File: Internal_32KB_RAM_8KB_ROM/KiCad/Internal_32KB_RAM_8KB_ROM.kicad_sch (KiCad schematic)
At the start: 12 parts, among them J1 UD4, J2 UE4, J3 RAM Decoder, J4 BLK Decoder, J5 Disable/Enable Switch, U1 ATF16V8, U2 74HCT138, U3 62256

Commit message: Redesigning
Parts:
- added C4: 100nF, Capacitor_THT:C_Disc_D3.0mm_W2.0mm_P2.50mm, symbol Device:C
- added U4: 2864, Package_DIP:DIP-28_W15.24mm, symbol Memory_EEPROM:KM28C64A
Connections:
- net +5V: now also C4.1, U4.27 (~{WE}), U4.28 (VCC)
- net BD0: now also U4.11 (I/O0)
- net BD1: now also U4.12 (I/O1)
- net BD2: now also U4.13 (I/O2)
- net BD3: now also U4.15 (I/O3)
- net BD4: now also U4.16 (I/O4)
- net BD5: now also U4.17 (I/O5)
- net BD6: now also U4.18 (I/O6)
- net BD7: now also U4.19 (I/O7)
- net GND: now also C4.2, U4.14 (GND), U4.22 (~{OE})
- net RAM_A13: now also U1.14 (I/O); no longer U1.13 (I/O)
- net RAM_A14: now also U1.15 (I/O); no longer U1.14 (I/O)
- net VA0: now also U4.10 (A0)
- net VA1: now also U4.9 (A1)
- net VA10: now also U4.21 (A10)
- net VA11: now also U4.23 (A11)
- net VA12: now also U4.2 (A12)
- net VA2: now also U4.8 (A2)
- net VA3: now also U4.7 (A3)
- net VA4: now also U4.6 (A4)
- net VA5: now also U4.5 (A5)
- net VA6: now also U4.4 (A6)
- net VA7: now also U4.3 (A7)
- net VA8: now also U4.25 (A8)
- net VA9: now also U4.24 (A9)
- net VR/~{W}: now also J1.10 (Pin_10); no longer J2.10 (Pin_10)
- net ~{BLK5_OUT}: now also U1.12 (I/O), U4.20 (~{CE}); no longer U1.15 (I/O)
- net ~{RAM_CS}: now also U1.13 (I/O); no longer U1.12 (I/O)
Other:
- note removed: "Future: To support ~{BLK5} expansion we will need to add an additional 6264"
- title: Commodore VIC-20 32KB RAM Expansion  -> Commodore VIC-20 32KB RAM+ROM Expansion 

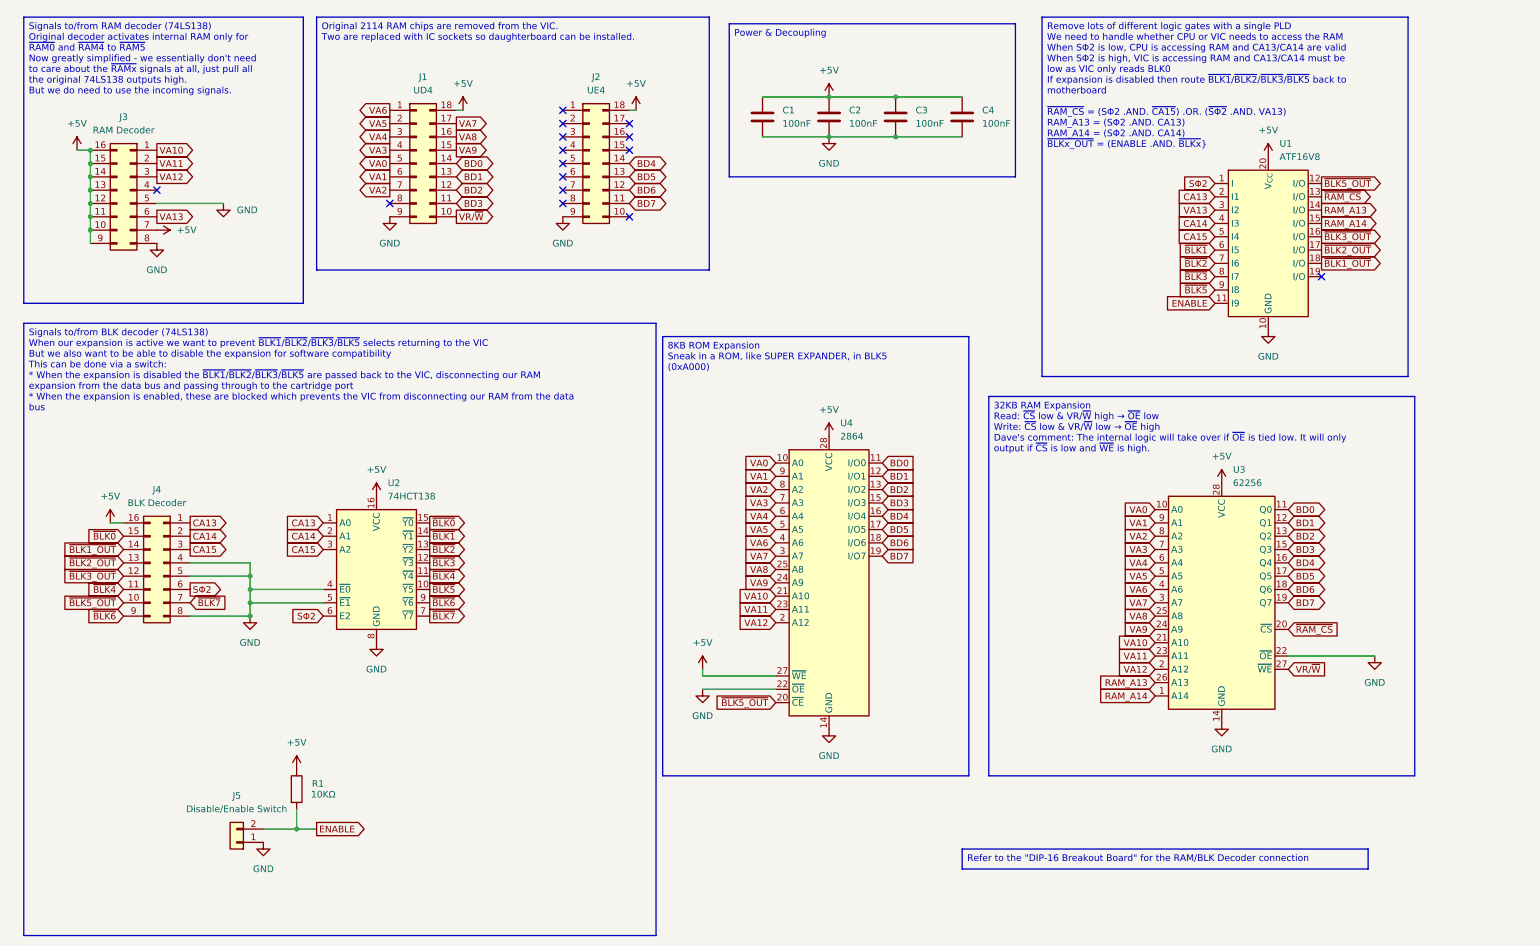
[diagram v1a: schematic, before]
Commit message: Finalised 40KB design for testing
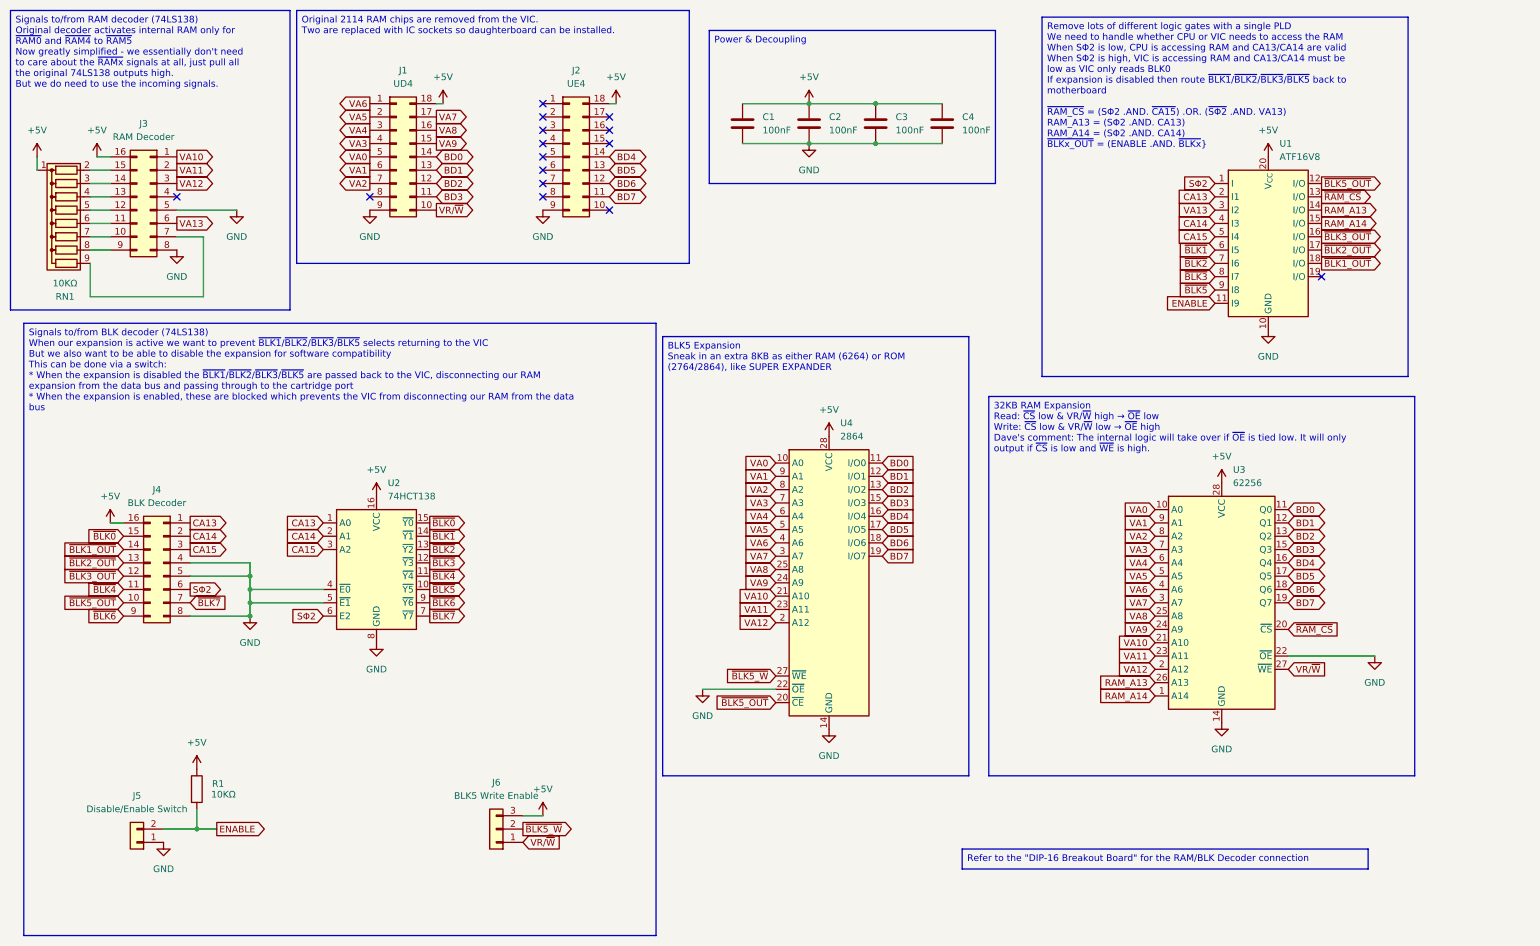
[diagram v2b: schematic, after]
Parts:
- added J6: BLK5 Write Enable, Connector_PinHeader_2.54mm:PinHeader_1x03_P2.54mm_Vertical, symbol Connector_Generic:Conn_01x03
- added RN1: 10KΩ, Resistor_THT:R_Array_SIP9, symbol Device:R_Network08
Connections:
- net +5V: now also J6.3 (Pin_3), RN1.1 (common); no longer J3.10 (Pin_10), J3.11 (Pin_11), J3.12 (Pin_12), J3.13 (Pin_13), J3.14 (Pin_14), J3.15 (Pin_15), J3.7 (Pin_7), J3.9 (Pin_9), U4.27 (~{WE})
- net VR/~{W}: now also J6.1 (Pin_1)
- new net: J3.10 (Pin_10), RN1.7 (R6)
- new net: J3.11 (Pin_11), RN1.6 (R5)
- new net: J3.12 (Pin_12), RN1.5 (R4)
- new net: J3.13 (Pin_13), RN1.4 (R3)
- new net: J3.14 (Pin_14), RN1.3 (R2)
- new net: J3.15 (Pin_15), RN1.2 (R1)
- new net: J3.7 (Pin_7), RN1.9 (R8)
- new net: J3.9 (Pin_9), RN1.8 (R7)
- new net ~{BLK5_W}: J6.2 (Pin_2), U4.27 (~{WE})
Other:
- title: Commodore VIC-20 32KB RAM+ROM Expansion  -> Commodore VIC-20 BLK0/1/2/3/5 Expansion 
- moved on the sheet: C1, C2, C3, C4, J1, J2, J3, J5, R1
